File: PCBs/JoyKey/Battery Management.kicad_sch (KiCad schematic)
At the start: 17 parts, among them J4 JST PH, Q1 PMOS,Si7157DP, U1 BQ25060, U4 LP2981-3.3

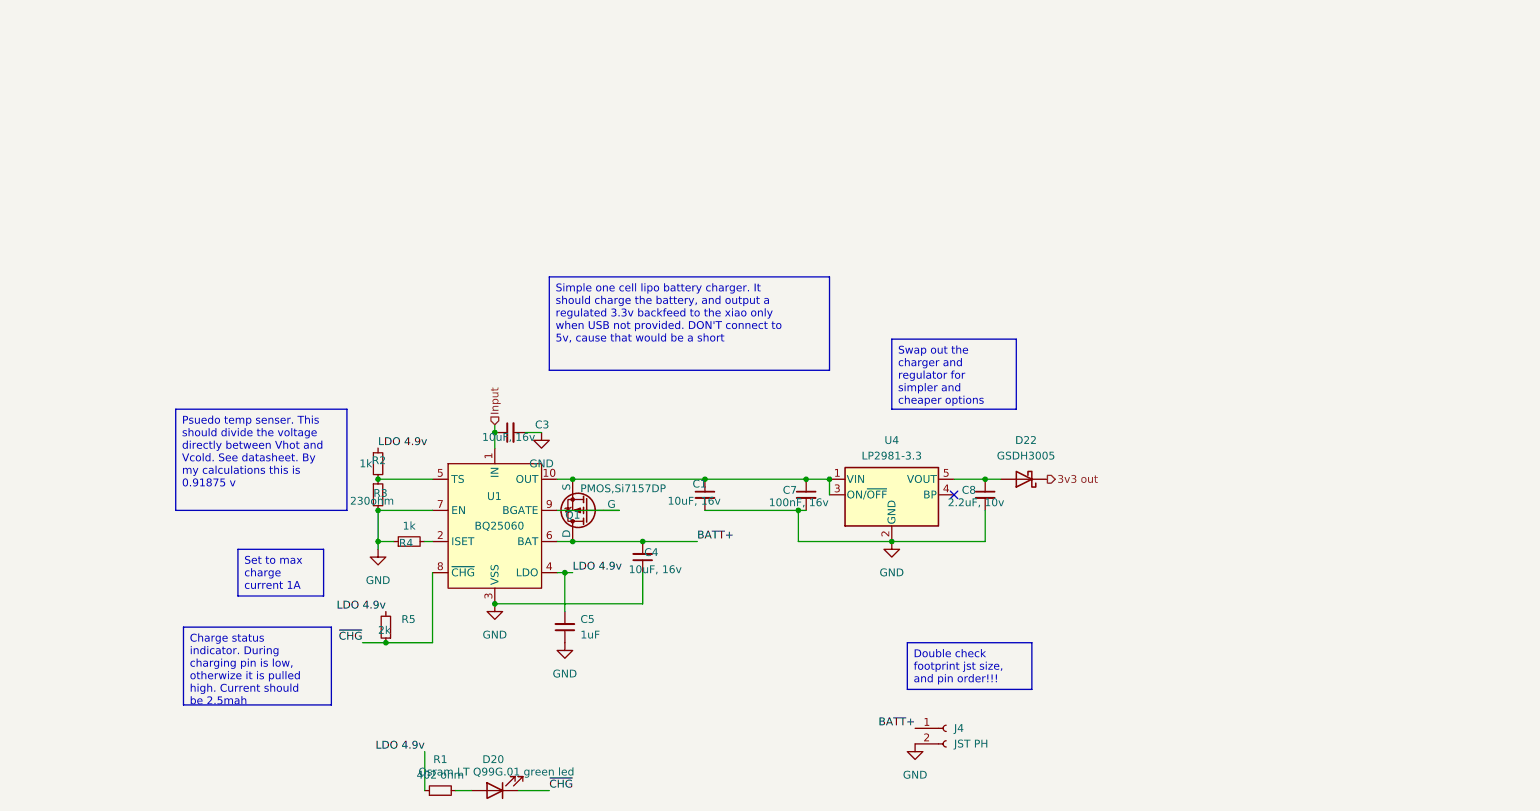
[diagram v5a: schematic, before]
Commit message: Updated Battery Management to Adafruit Feather system
I wanted to use a proven design that was low cost, and this seemed the best option. Only modification is removing the 5v input to the 3.3v regulator so that I don't have two regulators fighting
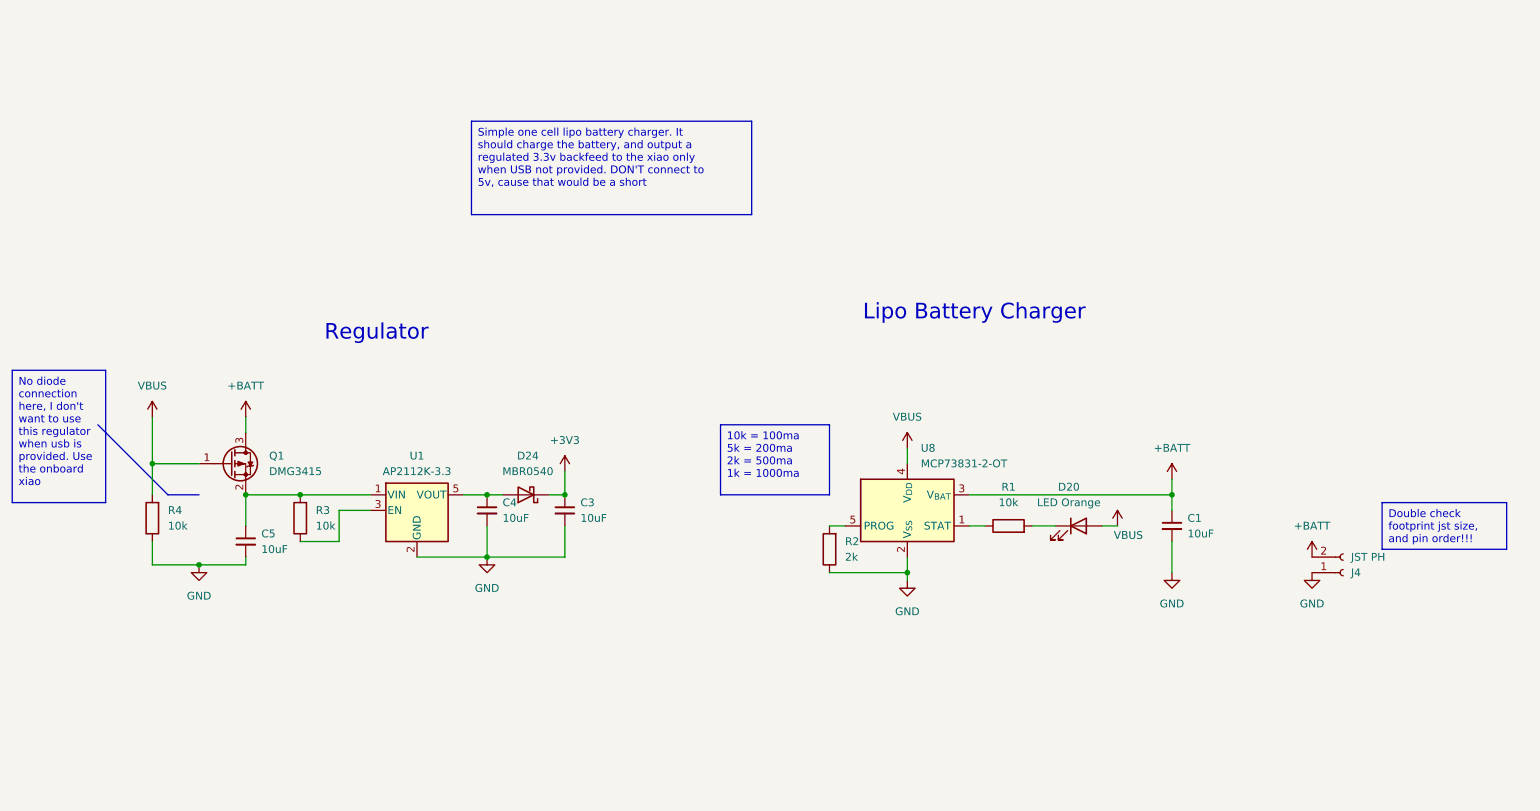
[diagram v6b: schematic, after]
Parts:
- removed C7: 100nF, 16v, Capacitor_SMD:C_0805_2012Metric, symbol Device:C_Small
- removed C8: 2.2uF, 10v, Capacitor_SMD:C_0805_2012Metric, symbol Device:C_Small
- removed D22: GSDH3005, Diode_SMD:D_0402_1005Metric, symbol Device:D_Schottky
- removed Q1: PMOS,Si7157DP, Package_DFN_QFN:PQFN-8-EP_6x5mm_P1.27mm_Generic, symbol Simulation_SPICE:PMOS
- removed R1: 402 ohm, Resistor_SMD:R_0805_2012Metric, symbol Device:R_Small
- removed R2, R4: 1k, Resistor_SMD:R_0805_2012Metric, symbol Device:R_Small
- removed R3: 230ohm, Resistor_SMD:R_0805_2012Metric, symbol Device:R_Small
- removed R5: 2k, Resistor_SMD:R_0805_2012Metric, symbol Device:R_Small
- removed U1: BQ25060, custom_Power:WSON-10-1EP_2x3mm_P0.5mm_EP0.84x2.4mm_ThermalVias_0.3mm, symbol custom_Battery_Management:BQ25060
- removed U4: LP2981-3.3, Package_TO_SOT_SMD:SOT-23-5, symbol Regulator_Linear:LP2985-3.3
- added D24: MBR0540, Diode_SMD:Nexperia_CFP3_SOD-123W, symbol Device:D_Schottky
- added Q1: DMG3415, Package_TO_SOT_SMD:SOT-23-5, symbol Device:Q_PMOS_GSD
- added R1, R3, R4: 10k, Resistor_SMD:R_0805_2012Metric, symbol Device:R
- added R2: 2k, Resistor_SMD:R_0805_2012Metric, symbol Device:R
- added U1: AP2112K-3.3, Package_TO_SOT_SMD:SOT-23-5, symbol Regulator_Linear:AP2112K-3.3
- added U8: MCP73831-2-OT, Package_TO_SOT_SMD:SOT-23-5, symbol Battery_Management:MCP73831-2-OT
- C1, C3, C4: value 10uF, 16v -> 10uF
- C5: value 1uF -> 10uF
- D20: value Osram LT Q99G.01 green led -> LED Orange; footprint LED_SMD:LED_0603_1608Metric_Pad1.05x0.95mm_HandSolder -> LED_SMD:LED_0603_1608Metric
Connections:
- net BATT+ is gone; now on net GND: C4.2, J4.1 (Pin_1)
- net LDO 4.9v is gone; now on net GND: C5.2
- net GND: now also R2.1, R4.1, U1.2 (GND), U8.2 (V_{SS}); no longer C4.1, C5.1, J4.2 (Pin_2)
- net +BATT: now reaches C1.1
- net +BATT: now also J4.2 (Pin_2), Q1.3 (D), U8.3 (V_{BAT})
- net VBUS: now reaches D20.2 (A)
- net VBUS: now also Q1.1 (G), R4.2, U8.4 (V_{DD})
- net Input renamed +3V3
- net +3V3: now also D24.1 (K)
- net ~{CHG}: no longer names the net of D20.1 (K)
- net ~{CHG}: now also R1.2
- new net: C4.1, D24.2 (A), U1.5 (VOUT)
- new net: C5.1, Q1.2 (S), R3.2, U1.1 (VIN)
- new net: R3.1, U1.3 (EN)
- new net: R1.1, U8.1 (STAT)
- new net: R2.2, U8.5 (PROG)
- no-connect marks 1 -> 0
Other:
- note added: "Lipo Battery Charger"
- note added: "Regulator"
- moved on the sheet: J4

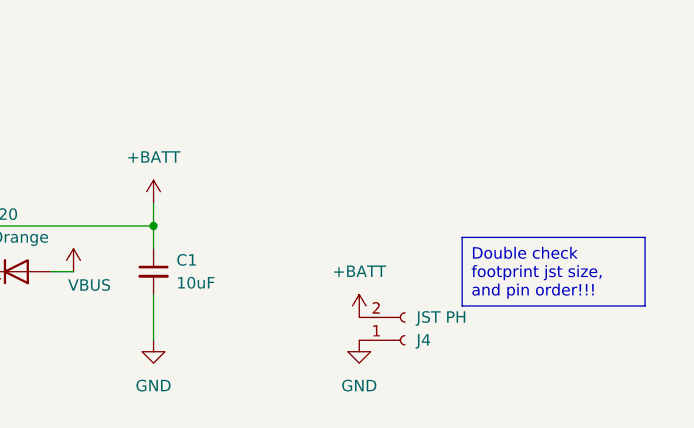
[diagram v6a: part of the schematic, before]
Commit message: Added JST mating point to connector
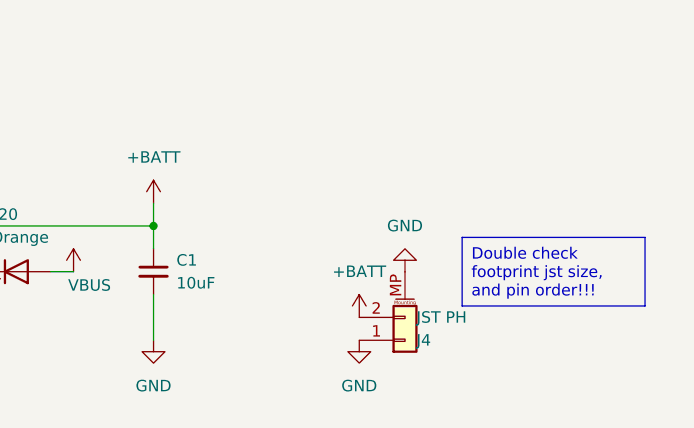
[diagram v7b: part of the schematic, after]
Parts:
- J4: symbol Connector:Conn_01x02_Socket -> Connector_Generic_MountingPin:Conn_01x02_MountingPin
- Q1: footprint Package_TO_SOT_SMD:SOT-23-5 -> Package_TO_SOT_SMD:SOT-23-3
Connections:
- net GND: now also J4.MP (MountPin)
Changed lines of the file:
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@@
+	)
+	(symbol
+		(lib_id "power:GND")
+		(at 254 114.3 180)
+		(unit 1)
+		(exclude_from_sim no)
+		(in_bom yes)
+		(on_board yes)
+		(dnp no)
+		(fields_autoplaced yes)
+		(property "Reference" "#PWR26"
+			(at 254 107.95 0)
+			(effects
+				(font
+					(size 1.27 1.27)
+				)
+				(hide yes)
+			)
+		)
+		(property "Value" "GND"
+			(at 254 109.22 0)
+			(effects
+				(font
+					(size 1.27 1.27)
+				)
+			)
+		)
+		(property "Footprint" ""
+			(at 254 114.3 0)
+			(effects
+				(font
+					(size 1.27 1.27)
+				)
+				(hide yes)
+			)
+		)
+		(property "Datasheet" ""
+			(at 254 114.3 0)
+			(effects
+				(font
+					(size 1.27 1.27)
+				)
+				(hide yes)
+			)
+		)
+		(property "Description" "Power symbol creates a global label with name \"GND\" , ground"
+			(at 254 114.3 0)
+			(effects
+				(font
+					(size 1.27 1.27)
+				)
+				(hide yes)
+			)
+		)
+		(pin "1"
+		)
+		(instances
+			(project "JoyKey"
+				(path "/7995ec7a-c14b-437e-b354-3eb74052b7cb/ac250670-848c-4fb5-87be-316f940b1e65"
+					(reference "#PWR26")
+					(unit 1)
+				)
+			)
+		)
 	)
 	(symbol
@@
 			)
 		)
-		(property "Footprint" "Package_TO_SOT_SMD:SOT-23-5"
+		(property "Footprint" "Package_TO_SOT_SMD:SOT-23-3"
 			(at 77.47 101.6 0)
 			(effects
@@
 	)
 	(symbol
-		(lib_id "Connector:Conn_01x02_Socket")
+		(lib_id "Connector_Generic_MountingPin:Conn_01x02_MountingPin")
 		(at 254 121.92 0)
 		(mirror x)
@@
 			)
 		)
-		(property "Description" "Generic connector, single row, 01x02, script generated"
+		(property "Description" "Generic connectable mounting pin connector, single row, 01x02, script generated (kicad-library-utils/schlib/autogen/connector/)"
 			(at 254 121.92 0)
 			(effects
@@
 		(pin "2"
 		)
-		(instances
+		(pin "MP"
+		)
+		(instances
